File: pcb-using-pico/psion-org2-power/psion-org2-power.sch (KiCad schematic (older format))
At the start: 14 parts, among them J1 Conn_02x08_Odd_Even, J2 Conn_02x08_Odd_Even, J3 Conn_01x27_Female, J4 Conn_02x08_Odd_Even, U6 74LS245, U7 74LS245

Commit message: Updates to both PCBs
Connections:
- net LS_DIR: now also J3.17 (Pin_17)
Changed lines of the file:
@@
 Wire Wire Line
 	11175 6225 10650 6225
+Text GLabel 1950 8175 2    50   Input ~ 0
+LS_DIR
 $EndSCHEMATC

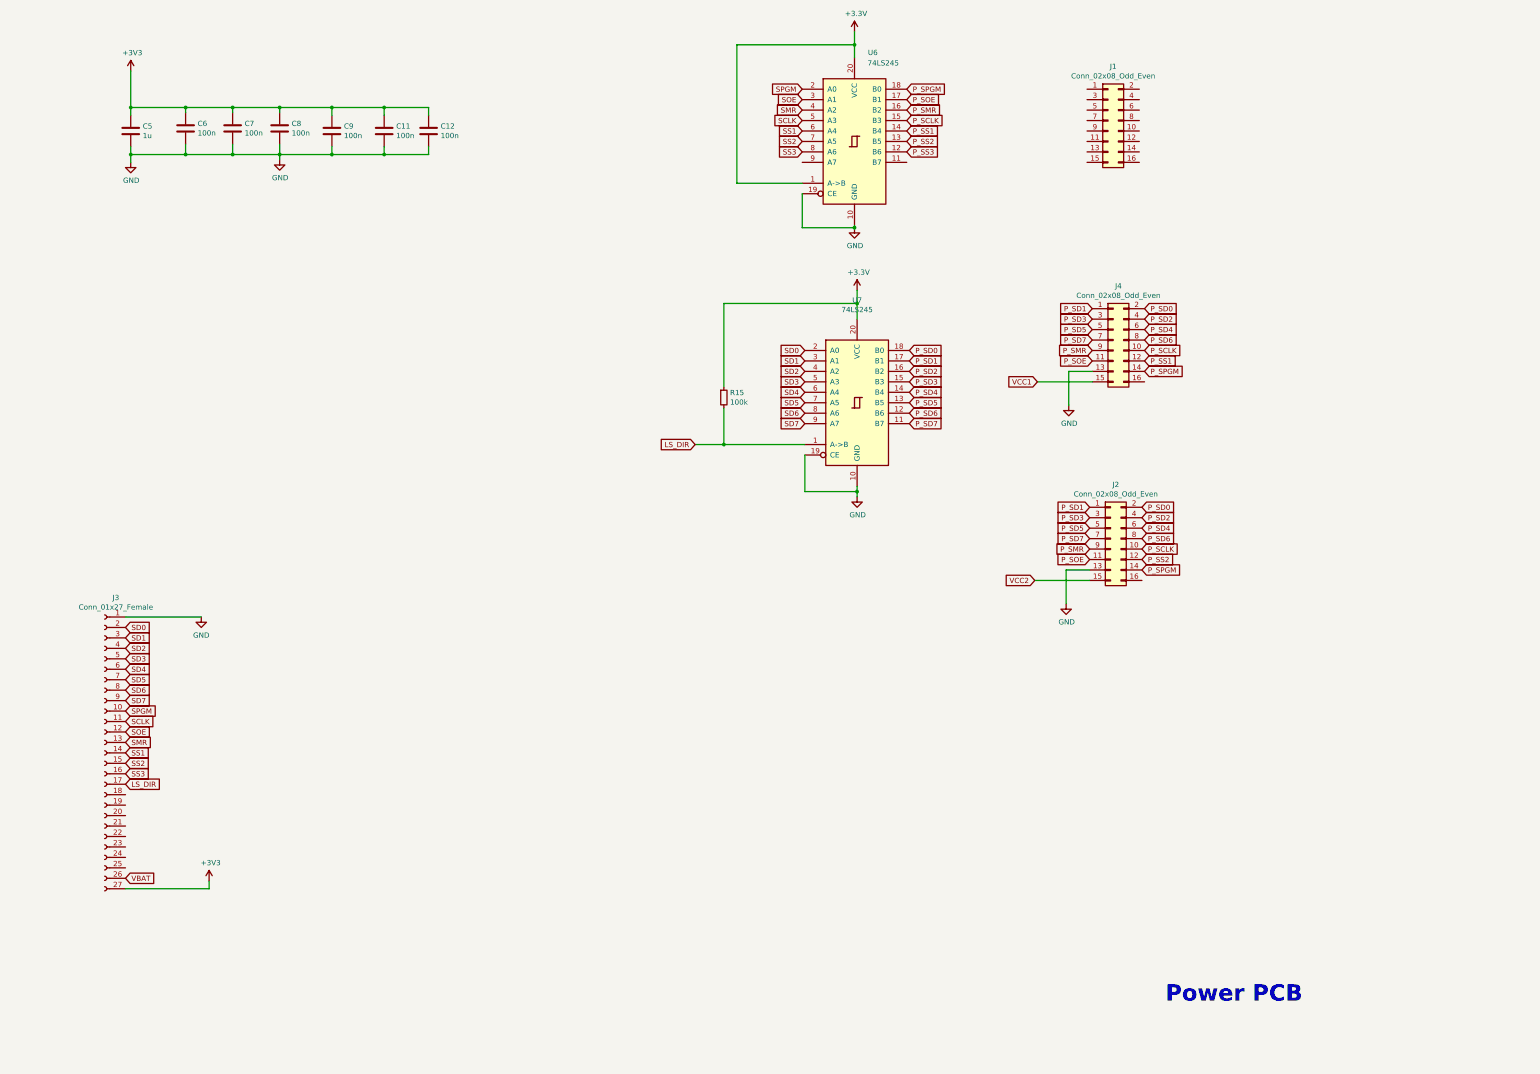
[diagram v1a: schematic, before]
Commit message: Added second connector, eeprom on power pcb
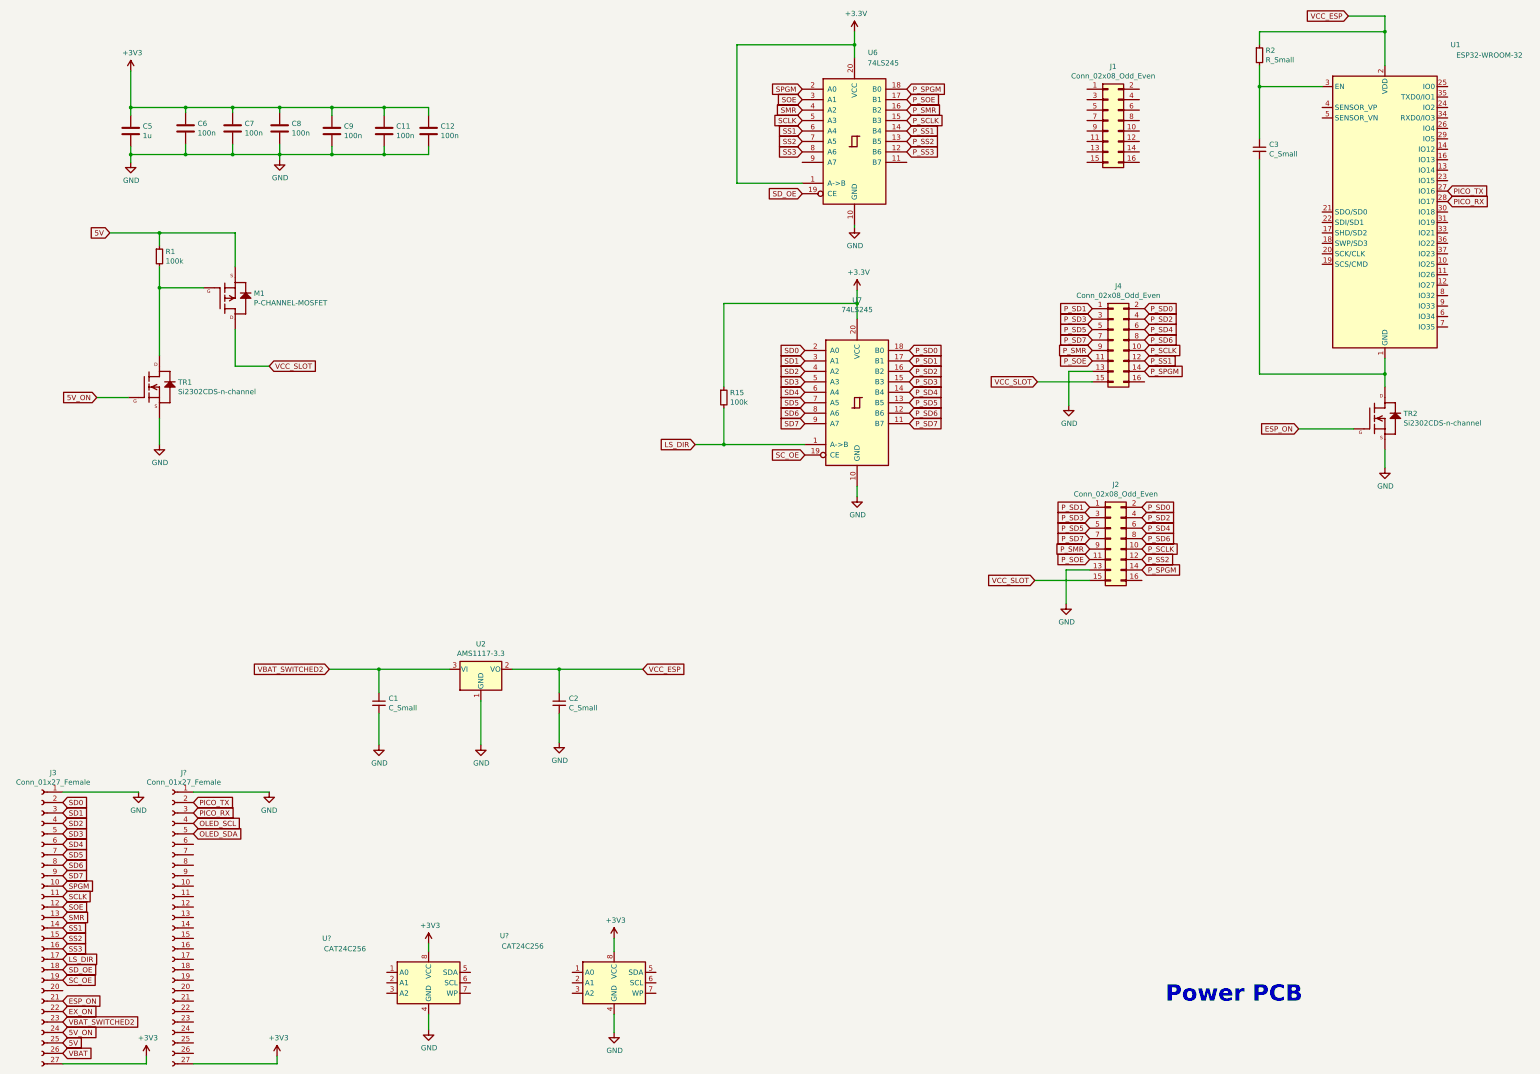
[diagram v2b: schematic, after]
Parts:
- added C1, C2, C3: C_Small, Capacitor_SMD:C_0805_2012Metric, symbol Device:C_Small
- added J?: Conn_01x27_Female, Connector_PinHeader_2.54mm:PinHeader_1x27_P2.54mm_Vertical, symbol Connector:Conn_01x27_Female
- added M1: P-CHANNEL-MOSFET, Package_TO_SOT_SMD:SOT-23, symbol GeekAmmo:P-CHANNEL-MOSFET
- added R1: 100k, Resistor_SMD:R_0805_2012Metric, symbol Device:R_Small
- added R2: R_Small, Resistor_SMD:R_0805_2012Metric, symbol Device:R_Small
- added TR1, TR2: Si2302CDS-n-channel, Package_TO_SOT_SMD:SOT-23, symbol New_Library:Si2302CDS-n-channel
- added U1: ESP32-WROOM-32, RF_Module:ESP32-WROOM-32, symbol RF_Module:ESP32-WROOM-32
- added U2: AMS1117-3.3, Package_TO_SOT_SMD:SOT-223-3_TabPin2, symbol pak_breakout:AMS1117-3.3
- added U? (x2): CAT24C256, symbol Memory_EEPROM:CAT24C256
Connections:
- net VCC2 is gone; now on net VCC_SLOT: J2.15 (Pin_15)
- net +3V3: now also J?.27 (Pin_27), U?.8 (VCC), U?.8 (VCC)
- net GND: now also C1.2, C2.2, J?.1 (Pin_1), TR1.2 (S), TR2.2 (S), U2.1 (GND), U?.4 (GND), U?.4 (GND); no longer U6.19 (CE), U7.19 (CE)
- net SD_OE: now reaches J3.18 (Pin_18)
- net SD_OE: now also U6.19 (CE)
- net SC_OE: now reaches J3.19 (Pin_19)
- net SC_OE: now also U7.19 (CE)
- net ESP_ON: now reaches J3.21 (Pin_21)
- net ESP_ON: now also TR2.1 (G)
- net EX_ON: now reaches J3.22 (Pin_22)
- net VBAT_SWITCHED2: now reaches J3.23 (Pin_23)
- net VBAT_SWITCHED2: now also C1.1, U2.3 (VI)
- net 5V_ON: now reaches J3.24 (Pin_24)
- net 5V_ON: now also TR1.1 (G)
- net 5V: now reaches J3.25 (Pin_25)
- net 5V: now also M1.2 (S), R1.1
- net VCC1 renamed VCC_SLOT
- net VCC_SLOT: now also M1.3 (D)
- new net: M1.1 (G), R1.2, TR1.3 (D)
- new net: C3.2, TR2.3 (D), U1.1 (GND), U1.15 (GND), U1.38 (GND), U1.39 (GND)
- new net: C3.1, R2.2, U1.3 (EN)
- new net OLED_SCL: J?.4 (Pin_4)
- new net OLED_SDA: J?.5 (Pin_5)
- new net PICO_RX: J?.3 (Pin_3), U1.28 (IO17)
- new net PICO_TX: J?.2 (Pin_2), U1.27 (IO16)
- new net VCC_ESP: C2.1, R2.1, U1.2 (VDD), U2.2 (VO)
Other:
- moved on the sheet: J3

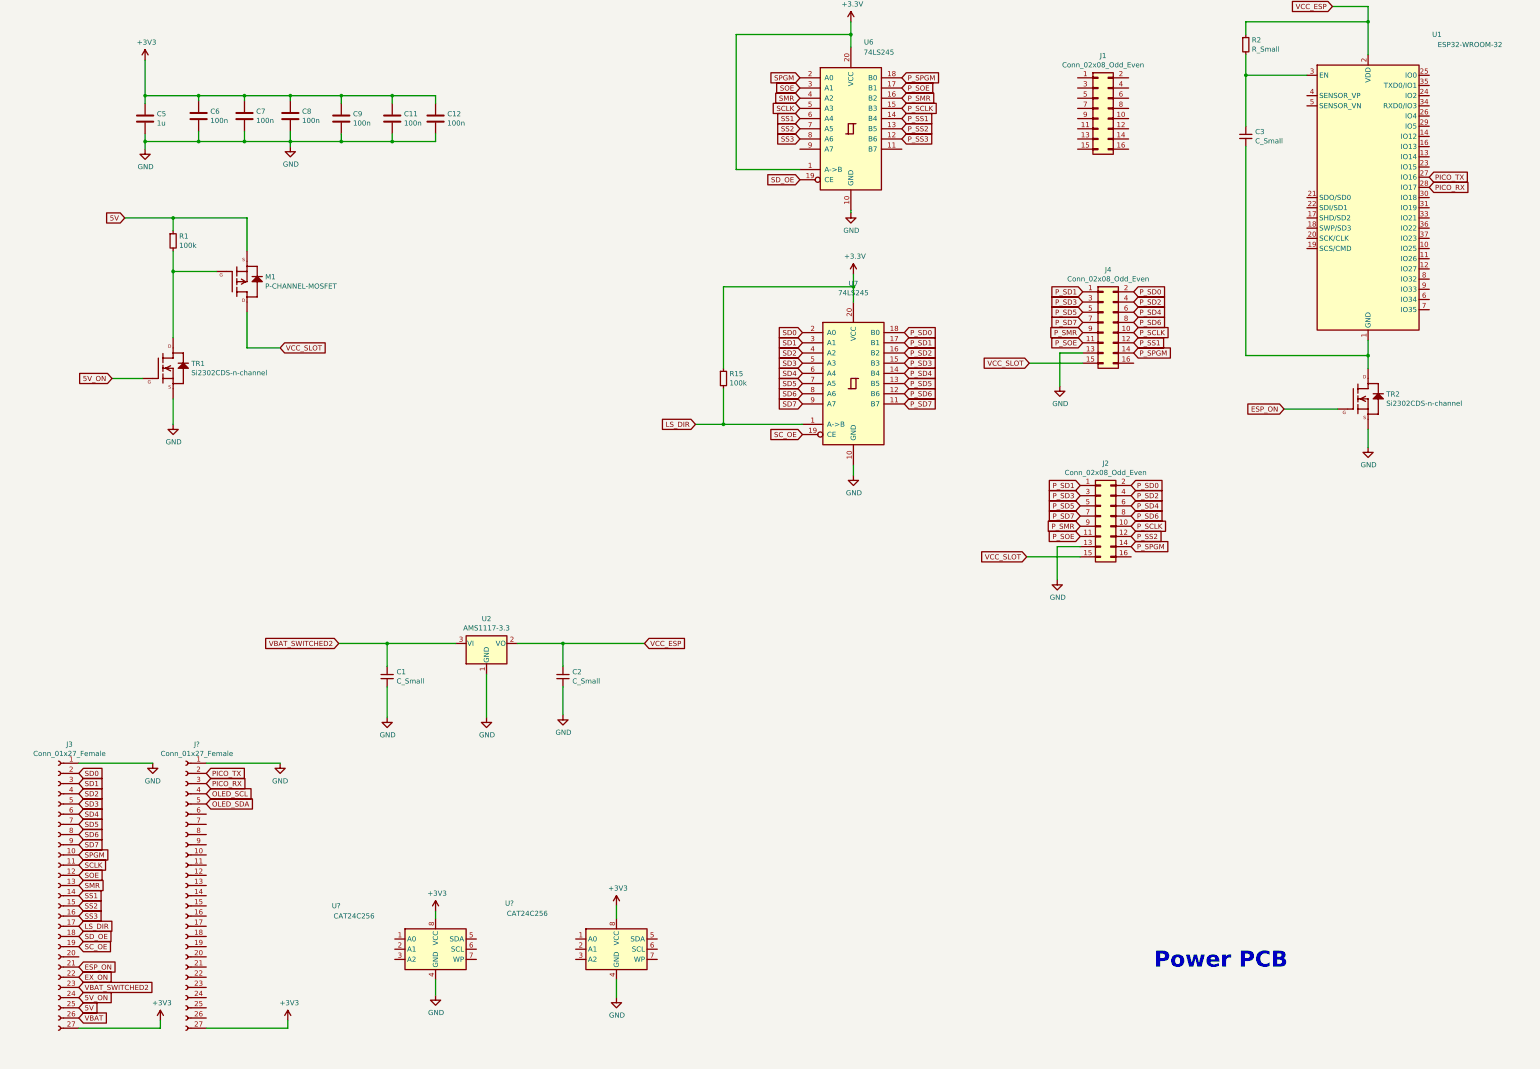
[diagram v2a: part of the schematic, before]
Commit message: Start of PCB layout
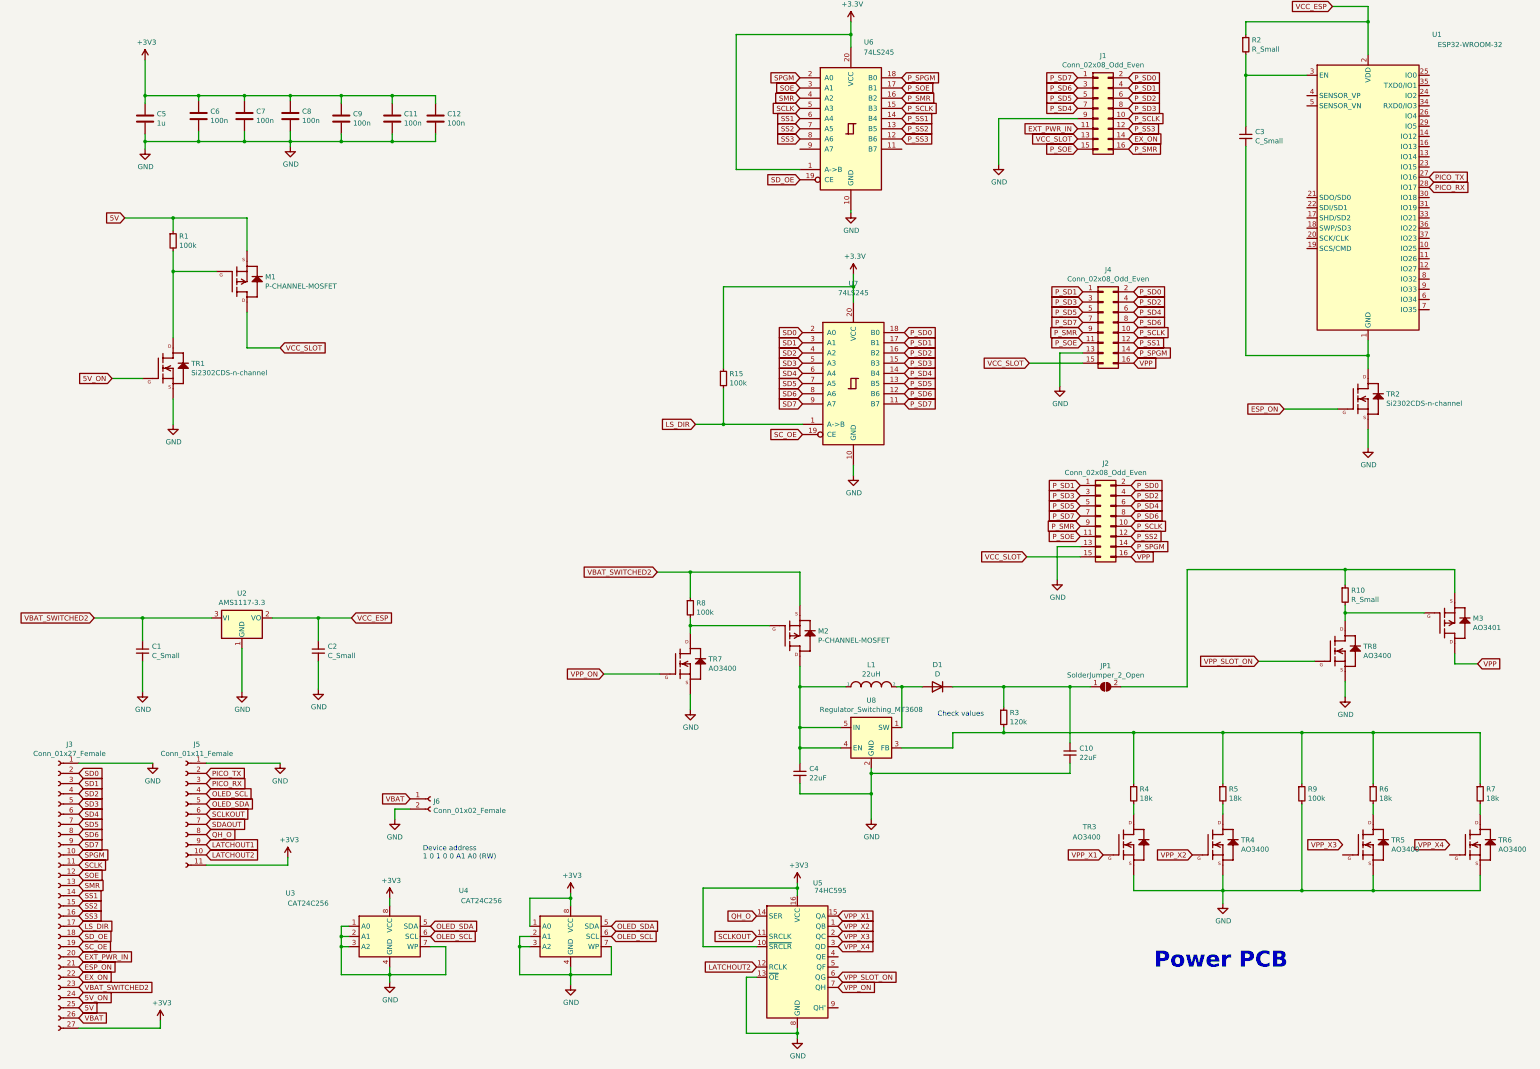
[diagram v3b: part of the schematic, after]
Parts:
- removed J?: Conn_01x27_Female, Connector_PinHeader_2.54mm:PinHeader_1x27_P2.54mm_Vertical, symbol Connector:Conn_01x27_Female
- added C10, C4: 22uF, Capacitor_SMD:C_1210_3225Metric_Pad1.42x2.65mm_HandSolder, symbol Device:C_Small
- added D1: D, Diode_SMD:D_SOD-123, symbol Device:D
- added J5: Conn_01x11_Female, Connector_PinHeader_2.54mm:PinHeader_1x11_P2.54mm_Vertical, symbol Connector:Conn_01x11_Female
- added J6: Conn_01x02_Female, Connector_PinHeader_2.54mm:PinHeader_1x02_P2.54mm_Vertical_SMD_Pin1Left, symbol Connector:Conn_01x02_Female
- added JP1: SolderJumper_2_Open, Jumper:SolderJumper-2_P1.3mm_Open_RoundedPad1.0x1.5mm, symbol Jumper:SolderJumper_2_Open
- added L1: 22uH, Inductor_SMD:L_Coilcraft_LPS5030, symbol pspice:INDUCTOR
- added M2: P-CHANNEL-MOSFET, Package_TO_SOT_SMD:SOT-23, symbol GeekAmmo:P-CHANNEL-MOSFET
- added M3: AO3401, Package_TO_SOT_SMD:SOT-23, symbol GeekAmmo:P-CHANNEL-MOSFET
- added R10: R_Small, Resistor_SMD:R_0805_2012Metric_Pad1.15x1.40mm_HandSolder, symbol Device:R_Small
- added R3: 120k, Resistor_SMD:R_0805_2012Metric_Pad1.15x1.40mm_HandSolder, symbol Device:R_Small
- added R4, R5, R6, R7: 18k, Resistor_SMD:R_0805_2012Metric_Pad1.15x1.40mm_HandSolder, symbol Device:R_Small
- added R8, R9: 100k, Resistor_SMD:R_0805_2012Metric_Pad1.15x1.40mm_HandSolder, symbol Device:R_Small
- added TR3, TR4, TR5, TR6, TR7, TR8: AO3400, Package_TO_SOT_SMD:SOT-23, symbol New_Library:Si2302CDS-n-channel
- added U5: 74HC595, Package_SO:SOIC-16_3.9x9.9mm_P1.27mm, symbol 74xx:74HC595
- added U8: Regulator_Switching_MT3608, Package_TO_SOT_SMD:SOT-23-6, symbol cq1re1-cache:Regulator_Switching_MT3608
- J2, J4: footprint Connector_PinHeader_2.54mm:PinHeader_2x08_P2.54mm_Horizontal -> ajm_kicad:PinHeader_2x08_P2.54mm_Horizontal_psionSide
- U3, U4: renamed from U?; footprint (none) -> Package_SO:SOIC-8_3.9x4.9mm_P1.27mm
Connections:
- net +3V3: now also U4.1 (A0), J5.11 (Pin_11), U5.10 (~SRCLR), U5.16 (VCC)
- net EX_ON: now also J1.14 (Pin_14)
- net GND: now also J1.9 (Pin_9), U3.1 (A0), U3.2 (A1), U3.3 (A2), U3.7 (WP), U4.2 (A1), U4.3 (A2), U4.7 (WP), C10.2, C4.2, J5.1 (Pin_1), J6.2 (Pin_2), R9.2, TR3.2 (S), TR4.2 (S), TR5.2 (S), TR6.2 (S), TR7.2 (S), TR8.2 (S), U5.13 (~OE), U5.8 (GND), U8.2 (GND)
- net OLED_SCL: now also U3.6 (SCL), U4.6 (SCL), J5.4 (Pin_4)
- net OLED_SDA: now also U3.5 (SDA), U4.5 (SDA), J5.5 (Pin_5)
- net PICO_RX: now also J5.3 (Pin_3)
- net PICO_TX: now also J5.2 (Pin_2)
- net P_SCLK: now also J1.10 (Pin_10)
- net P_SD0: now also J1.2 (Pin_2)
- net P_SD1: now also J1.4 (Pin_4)
- net P_SD2: now also J1.6 (Pin_6)
- net P_SD3: now also J1.8 (Pin_8)
- net P_SD4: now also J1.7 (Pin_7)
- net P_SD5: now also J1.5 (Pin_5)
- net P_SD6: now also J1.3 (Pin_3)
- net P_SD7: now also J1.1 (Pin_1)
- net P_SMR: now also J1.16 (Pin_16)
- net P_SOE: now also J1.15 (Pin_15)
- net P_SS3: now also J1.12 (Pin_12)
- net VBAT: now also J6.1 (Pin_1)
- net VBAT_SWITCHED2: now also M2.2 (S), R8.1
- net VCC_SLOT: now also J1.13 (Pin_13)
- net EXT_PWR_IN: now reaches J1.11 (Pin_11)
- net EXT_PWR_IN: now also J3.20 (Pin_20)
- net VPP: now reaches J4.16 (Pin_16)
- net VPP: now also J2.16 (Pin_16), M3.3 (D)
- new net: R3.2, R4.1, R5.1, R6.1, R7.1, R9.1, U8.3 (FB)
- new net: R5.2, TR4.3 (D)
- new net: C4.1, L1.1, M2.3 (D), U8.4 (EN), U8.5 (IN)
- new net: C10.1, D1.1 (K), JP1.1 (A), R3.1
- new net: D1.2 (A), L1.2, U8.1 (SW)
- new net: JP1.2 (B), M3.2 (S), R10.1
- new net: M2.1 (G), R8.2, TR7.3 (D)
- new net: R4.2, TR3.3 (D)
- new net: R6.2, TR5.3 (D)
- new net: R7.2, TR6.3 (D)
- new net: M3.1 (G), R10.2, TR8.3 (D)
- new net LATCHOUT1: J5.9 (Pin_9)
- new net LATCHOUT2: J5.10 (Pin_10), U5.12 (RCLK)
- new net QH_O: J5.8 (Pin_8), U5.14 (SER)
- new net SCLKOUT: J5.6 (Pin_6), U5.11 (SRCLK)
- new net SDAOUT: J5.7 (Pin_7)
- new net VPP_ON: TR7.1 (G), U5.7 (QH)
- new net VPP_SLOT_ON: TR8.1 (G), U5.6 (QG)
- new net VPP_X1: TR3.1 (G), U5.15 (QA)
- new net VPP_X2: TR4.1 (G), U5.1 (QB)
- new net VPP_X3: U5.2 (QC)
- new net VPP_X4: U5.3 (QD)
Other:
- note added: "Check values\n"
- note added: "Device address\n1 0 1 0 0 A1 A0 (RW)\n"
- moved on the sheet: C1, C2, U2, U3, U4
